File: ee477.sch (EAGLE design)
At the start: 2 parts

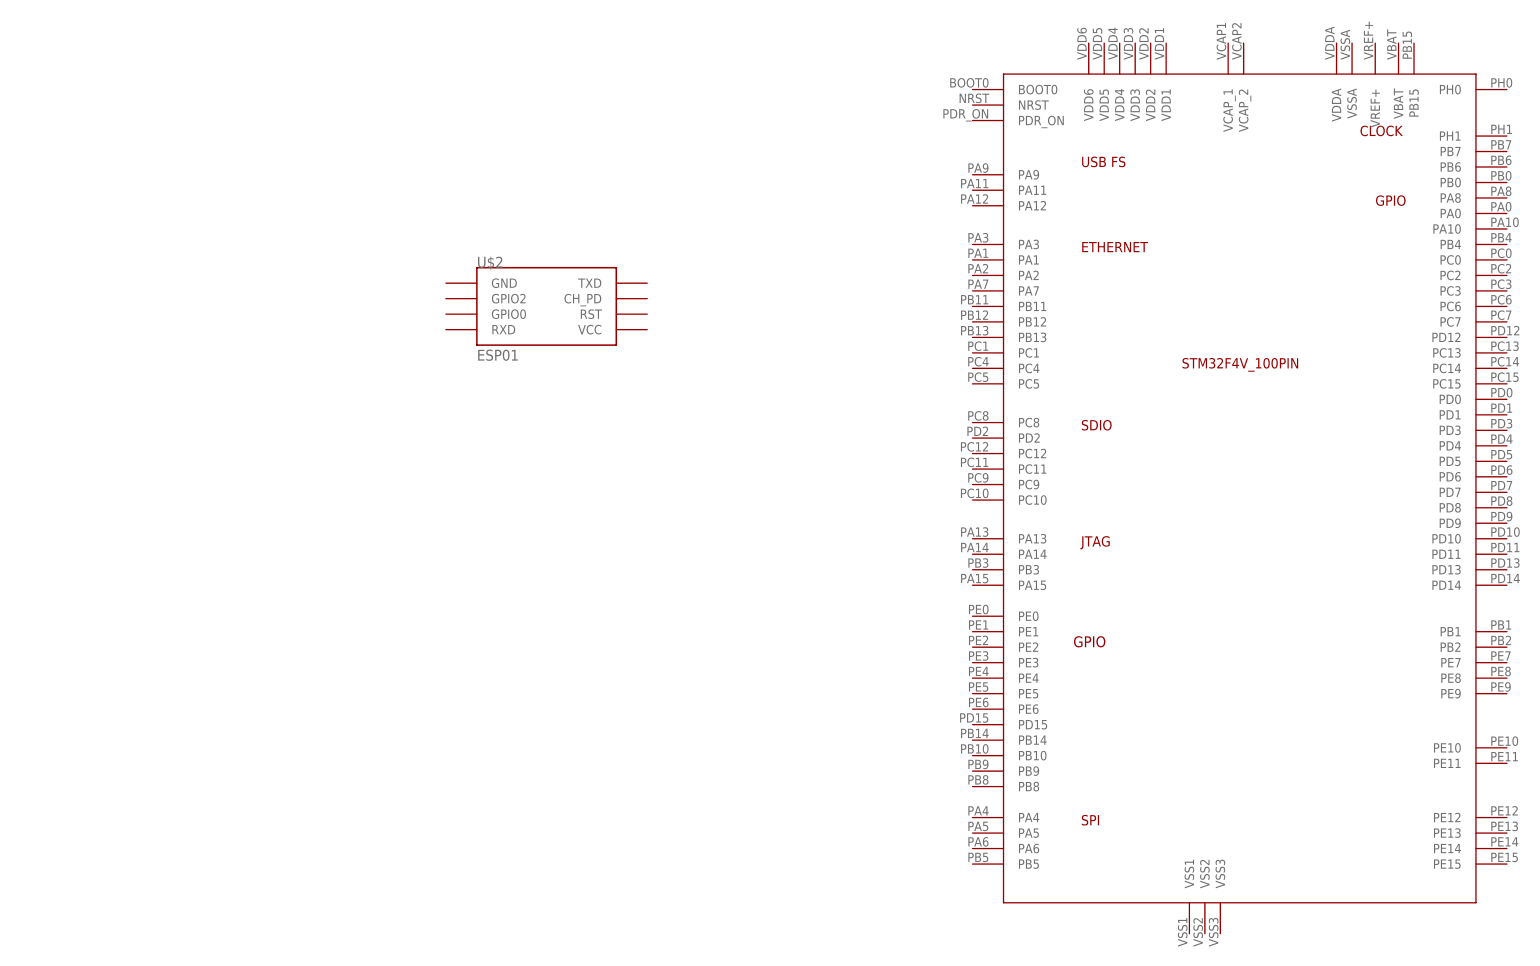
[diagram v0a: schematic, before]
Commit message: added esp prog&rst circuit
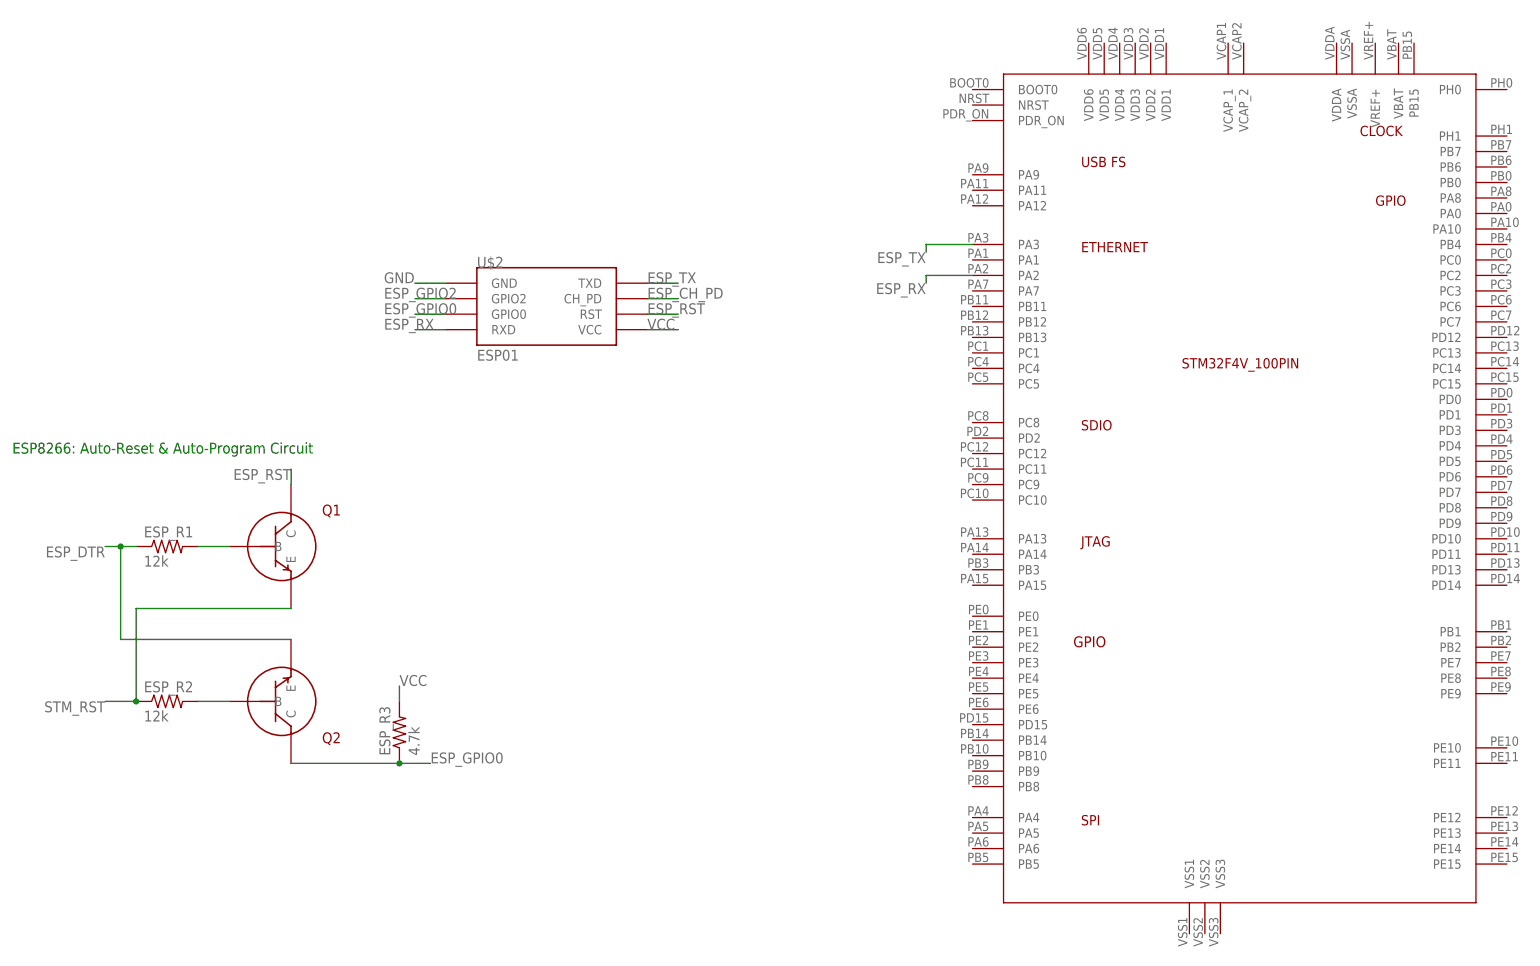
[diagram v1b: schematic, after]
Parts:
- added ESP_R1, ESP_R2: 12k, rcl:R-US_1812X7R
- added ESP_R3: 4.7k, rcl:R-US_1812X7R
- added Q1, Q2: (no value), ngspice-simulation:BJT_NPN
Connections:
- new net ESP_CH_PD: U$2.CH_PD
- new net ESP_DTR: ESP_R1.1, Q2.E
- new net ESP_GPIO0: ESP_R3.1, Q2.C, U$2.GPIO0
- new net ESP_GPIO2: U$2.GPIO2
- new net ESP_RST: Q1.C, U$2.RST
- new net ESP_RX: U$1.PA2, U$2.RXD
- new net ESP_TX: U$1.PA3, U$2.TXD
- new net GND: U$2.GND
- new net N$1: ESP_R2.2, Q2.B
- new net N$2: ESP_R1.2, Q1.B
- new net STM_RST: ESP_R2.1, Q1.E
- new net VCC: ESP_R3.2, U$2.VCC
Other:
- note added: "ESP8266: Auto-Reset & Auto-Program Circuit"
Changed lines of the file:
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@@
 <layer number="97" name="Info" color="7" fill="1" visible="yes" active="yes"/>
 <layer number="98" name="Guide" color="6" fill="1" visible="yes" active="yes"/>
+<layer number="99" name="SpiceOrder" color="7" fill="1" visible="yes" active="yes"/>
 </layers>
 <schematic xreflabel="%F%N/%S.%C%R" xrefpart="/%S.%C%R">
@@
 <part name="U$1" library="stm32f4" deviceset="STM32F4V_100PIN_GPSBOARD" device=""/>
 <part name="U$2" library="esp8266modules" deviceset="ESP01" device=""/>
+<part name="ESP_R1" library="rcl" library_urn="urn:adsk.eagle:library:334" deviceset="R-US_" device="1812X7R" package3d_urn="urn:adsk.eagle:package:23609/1" value="12k"/>
+<part name="ESP_R2" library="rcl" library_urn="urn:adsk.eagle:library:334" deviceset="R-US_" device="1812X7R" package3d_urn="urn:adsk.eagle:package:23609/1" value="12k"/>
+<part name="ESP_R3" library="rcl" library_urn="urn:adsk.eagle:library:334" deviceset="R-US_" device="1812X7R" package3d_urn="urn:adsk.eagle:package:23609/1" value="4.7k"/>
+<part name="Q1" library="ngspice-simulation" library_urn="urn:adsk.eagle:library:527439" deviceset="BJT_NPN" device=""/>
+<part name="Q2" library="ngspice-simulation" library_urn="urn:adsk.eagle:library:527439" deviceset="BJT_NPN" device=""/>
 </parts>
 <sheets>
 <sheet>
 <plain>
+<text x="-149.86" y="81.28" size="1.778" layer="91">ESP8266: Auto-Reset &amp; Auto-Program Circuit</text>
 </plain>
 <instances>
 <instance part="U$1" gate="G$1" x="50.8" y="91.44"/>
 <instance part="U$2" gate="G$1" x="-60.96" y="101.6"/>
+<instance part="ESP_R1" gate="G$1" x="-124.46" y="66.04"/>
+<instance part="ESP_R2" gate="G$1" x="-124.46" y="40.64"/>
+<instance part="ESP_R3" gate="G$1" x="-86.36" y="35.56" rot="R90"/>
+<instance part="Q1" gate="G$1" x="-114.3" y="66.04"/>
+<instance part="Q2" gate="G$1" x="-114.3" y="40.64" rot="MR180"/>
 </instances>
 <busses>
 </busses>
 <nets>
+<net name="ESP_TX" class="0">
+<segment>
+<pinref part="U$2" gate="G$1" pin="TXD"/>
+<wire x1="-45.72" y1="109.22" x2="-40.64" y2="109.22" width="0.1524" layer="91"/>
+<label x="-45.72" y="109.22" size="1.778" layer="95"/>
+</segment>
+<segment>
+<pinref part="U$1" gate="G$1" pin="PA3"/>
+<wire x1="7.62" y1="115.57" x2="0" y2="115.57" width="0.1524" layer="91"/>
+<wire x1="0" y1="115.57" x2="0" y2="114.3" width="0.1524" layer="91"/>
+<label x="0" y="114.3" size="1.778" layer="95" rot="R180"/>
+</segment>
+</net>
+<net name="ESP_CH_PD" class="0">
+<segment>
+<pinref part="U$2" gate="G$1" pin="CH_PD"/>
+<wire x1="-45.72" y1="106.68" x2="-40.64" y2="106.68" width="0.1524" layer="91"/>
+<label x="-45.72" y="106.68" size="1.778" layer="95"/>
+</segment>
+</net>
+<net name="ESP_RST" class="0">
+<segment>
+<pinref part="U$2" gate="G$1" pin="RST"/>
+<wire x1="-45.72" y1="104.14" x2="-40.64" y2="104.14" width="0.1524" layer="91"/>
+<label x="-45.72" y="104.14" size="1.778" layer="95"/>
+</segment>
+<segment>
+<pinref part="Q1" gate="G$1" pin="C"/>
+<wire x1="-104.14" y1="76.2" x2="-104.14" y2="78.74" width="0.1524" layer="91"/>
+<label x="-104.14" y="78.74" size="1.778" layer="95" rot="R180"/>
+</segment>
+</net>
+<net name="VCC" class="0">
+<segment>
+<pinref part="U$2" gate="G$1" pin="VCC"/>
+<wire x1="-45.72" y1="101.6" x2="-40.64" y2="101.6" width="0.1524" layer="91"/>
+<label x="-45.72" y="101.6" size="1.778" layer="95"/>
+</segment>
+<segment>
+<pinref part="ESP_R3" gate="G$1" pin="2"/>
+<wire x1="-86.36" y1="40.64" x2="-86.36" y2="43.18" width="0.1524" layer="91"/>
+<label x="-86.36" y="43.18" size="1.778" layer="95"/>
+</segment>
+</net>
+<net name="GND" class="0">
+<segment>
+<pinref part="U$2" gate="G$1" pin="GND"/>
+<wire x1="-78.74" y1="109.22" x2="-83.82" y2="109.22" width="0.1524" layer="91"/>
+<label x="-88.9" y="109.22" size="1.778" layer="95"/>
+</segment>
+</net>
+<net name="ESP_GPIO2" class="0">
+<segment>
+<pinref part="U$2" gate="G$1" pin="GPIO2"/>
+<wire x1="-78.74" y1="106.68" x2="-83.82" y2="106.68" width="0.1524" layer="91"/>
+<label x="-88.9" y="106.68" size="1.778" layer="95"/>
+</segment>
+</net>
+<net name="ESP_GPIO0" class="0">
+<segment>
+<pinref part="U$2" gate="G$1" pin="GPIO0"/>
+<wire x1="-78.74" y1="104.14" x2="-83.82" y2="104.14" width="0.1524" layer="91"/>
+<label x="-88.9" y="104.14" size="1.778" layer="95"/>
+</segment>
+<segment>
+<pinref part="Q2" gate="G$1" pin="C"/>
+<pinref part="ESP_R3" gate="G$1" pin="1"/>
+<wire x1="-104.14" y1="30.48" x2="-86.36" y2="30.48" width="0.1524" layer="91"/>
+<wire x1="-86.36" y1="30.48" x2="-81.28" y2="30.48" width="0.1524" layer="91"/>
+<junction x="-86.36" y="30.48"/>
+<label x="-81.28" y="30.48" size="1.778" layer="95"/>
+</segment>
+</net>
+<net name="ESP_RX" class="0">
+<segment>
+<pinref part="U$2" gate="G$1" pin="RXD"/>
+<wire x1="-78.74" y1="101.6" x2="-83.82" y2="101.6" width="0.1524" layer="91"/>
+<label x="-88.9" y="101.6" size="1.778" layer="95"/>
+</segment>
+<segment>
+<pinref part="U$1" gate="G$1" pin="PA2"/>
+<wire x1="7.62" y1="110.49" x2="0" y2="110.49" width="0.1524" layer="91"/>
+<wire x1="0" y1="110.49" x2="0" y2="109.22" width="0.1524" layer="91"/>
+<label x="0" y="109.22" size="1.778" layer="95" rot="R180"/>
+</segment>
+</net>
+<net name="N$1" class="0">
+<segment>
+<pinref part="Q2" gate="G$1" pin="B"/>
+<pinref part="ESP_R2" gate="G$1" pin="2"/>
+<wire x1="-119.38" y1="40.64" x2="-114.3" y2="40.64" width="0.1524" layer="91"/>
+</segment>
+</net>
+<net name="N$2" class="0">
+<segment>
+<pinref part="Q1" gate="G$1" pin="B"/>
+<pinref part="ESP_R1" gate="G$1" pin="2"/>
+<wire x1="-119.38" y1="66.04" x2="-114.3" y2="66.04" width="0.1524" layer="91"/>
+</segment>
+</net>
+<net name="ESP_DTR" class="0">
+<segment>
+<pinref part="ESP_R1" gate="G$1" pin="1"/>
+<wire x1="-129.54" y1="66.04" x2="-132.08" y2="66.04" width="0.1524" layer="91"/>
+<pinref part="Q2" gate="G$1" pin="E"/>
+<wire x1="-132.08" y1="66.04" x2="-134.62" y2="66.04" width="0.1524" layer="91"/>
+<wire x1="-132.08" y1="66.04" x2="-132.08" y2="50.8" width="0.1524" layer="91"/>
+<wire x1="-132.08" y1="50.8" x2="-104.14" y2="50.8" width="0.1524" layer="91"/>
+<junction x="-132.08" y="66.04"/>
+<label x="-134.62" y="66.04" size="1.778" layer="95" rot="R180"/>
+</segment>
+</net>
+<net name="STM_RST" class="0">
+<segment>
+<pinref part="ESP_R2" gate="G$1" pin="1"/>
+<wire x1="-129.54" y1="40.64" x2="-134.62" y2="40.64" width="0.1524" layer="91"/>
+<pinref part="Q1" gate="G$1" pin="E"/>
+<wire x1="-104.14" y1="55.88" x2="-129.54" y2="55.88" width="0.1524" layer="91"/>
+<wire x1="-129.54" y1="55.88" x2="-129.54" y2="40.64" width="0.1524" layer="91"/>
+<junction x="-129.54" y="40.64"/>
+<label x="-134.62" y="40.64" size="1.778" layer="95" rot="R180"/>
+</segment>
+</net>
 </nets>
 </sheet>
@@
 </schematic>
 </drawing>
+<compatibility>
+<note version="8.2" severity="warning">
+Since Version 8.2, EAGLE supports online libraries. The ids
+of those online libraries will not be understood (or retained)
+with this version.
+</note>
+<note version="8.3" severity="warning">
+Since Version 8.3, EAGLE supports URNs for individual library
+assets (packages, symbols, and devices). The URNs of those assets
+will not be understood (or retained) with this version.
+</note>
+<note version="8.3" severity="warning">
+Since Version 8.3, EAGLE supports the association of 3D packages
+with devices in libraries, schematics, and board files. Those 3D
+packages will not be understood (or retained) with this version.
+</note>
+<note version="8.4" severity="warning">
+Since Version 8.4, EAGLE supports properties for SPICE simulation.
+Probes in schematics and SPICE mapping objects found in parts and library devices
+will not be understood with this version. Update EAGLE to the latest version
+for full support of SPICE simulation.
+</note>
+</compatibility>
 </eagle>
